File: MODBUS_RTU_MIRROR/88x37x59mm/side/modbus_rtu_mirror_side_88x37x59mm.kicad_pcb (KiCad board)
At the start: 2 copper layers, 52 x 40 mm, 5 parts, among them J1 Conn_01x04_Male, J2 Conn_01x04_Male, U1 ESP32-WROOM-32, U2 TXS0108EPW, U3 AMS1117-3.3

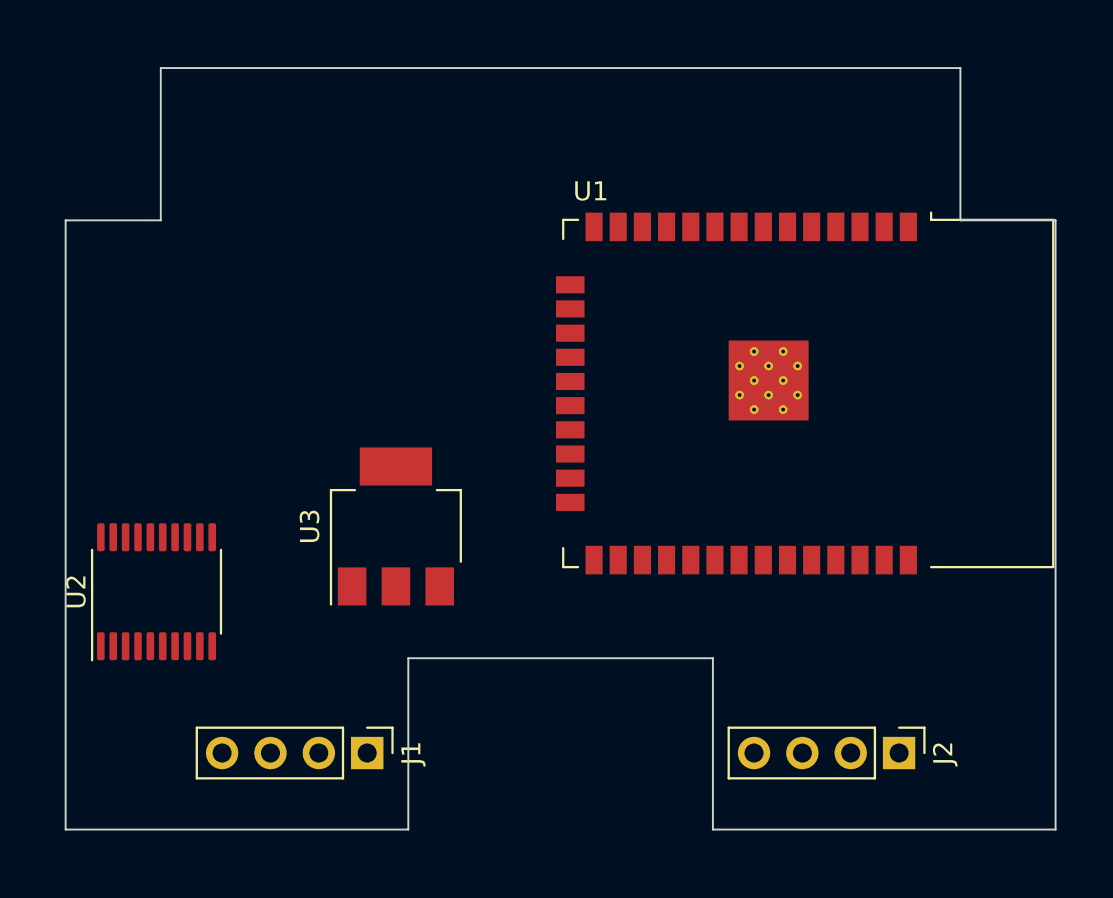
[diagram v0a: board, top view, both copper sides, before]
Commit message: added capacitors, rtc, prog header
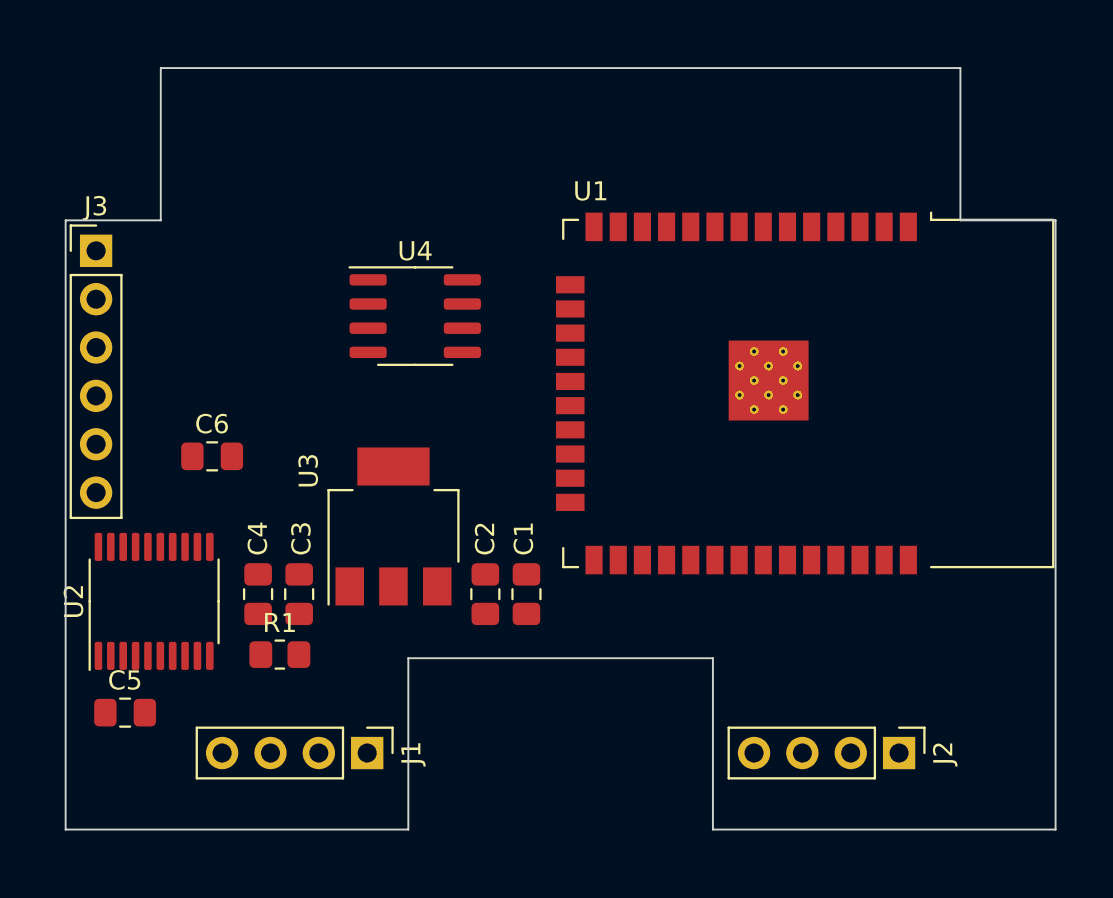
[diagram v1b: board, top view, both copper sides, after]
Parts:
- added C1: 100nF, Capacitor_SMD:C_0805_2012Metric_Pad1.18x1.45mm_HandSolder, F.Cu at (124.2, 127.6)
- added C2: 22uF, Capacitor_SMD:C_0805_2012Metric_Pad1.18x1.45mm_HandSolder, F.Cu at (122.0, 127.6)
- added C3: 22uF, Capacitor_SMD:C_0805_2012Metric_Pad1.18x1.45mm_HandSolder, F.Cu at (112.3, 127.6)
- added C4: 100nF, Capacitor_SMD:C_0805_2012Metric_Pad1.18x1.45mm_HandSolder, F.Cu at (110.1, 127.6)
- added C5: 100nF, Capacitor_SMD:C_0805_2012Metric_Pad1.18x1.45mm_HandSolder, F.Cu at (103.1, 133.9)
- added C6: 100nF, Capacitor_SMD:C_0805_2012Metric_Pad1.18x1.45mm_HandSolder, F.Cu at (107.7, 120.4)
- added J3: Conn_01x06_Male, Connector_PinHeader_2.54mm:PinHeader_1x06_P2.54mm_Vertical, F.Cu at (101.6, 109.6)
- added R1: R, Resistor_SMD:R_0805_2012Metric_Pad1.20x1.40mm_HandSolder, F.Cu at (111.3, 130.8)
- added U4: DS3231MZ, Package_SO:SOIC-8_3.9x4.9mm_P1.27mm, F.Cu at (118.4, 113.0)
- moved U2 0.52 mm to (104.6, 128.0)
- moved U3 0.13 mm to (117.2, 124.1)
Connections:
- U2 pad 10: unconnected-(U2-Pad10) -> Net-(U2-Pad10)

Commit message: added leds and pushbutton
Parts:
- added D1: LED, LED_THT:LED_D3.0mm, F.Cu at (141.7, 104.3)
- added D2: LED, LED_THT:LED_D3.0mm, F.Cu at (136.6, 104.3)
- added D3: LED, LED_THT:LED_D3.0mm, F.Cu at (131.5, 104.3)
- added D4: LED, LED_THT:LED_D3.0mm, F.Cu at (126.4, 104.3)
- added D5: LED, LED_THT:LED_D3.0mm, F.Cu at (121.3, 104.3)
- added D6: LED, LED_THT:LED_D3.0mm, F.Cu at (116.2, 104.3)
- added SW1: SW_Push, Button_Switch_THT:SW_Tactile_SPST_Angled_PTS645Vx31-2LFS, F.Cu at (107.6, 102.9)

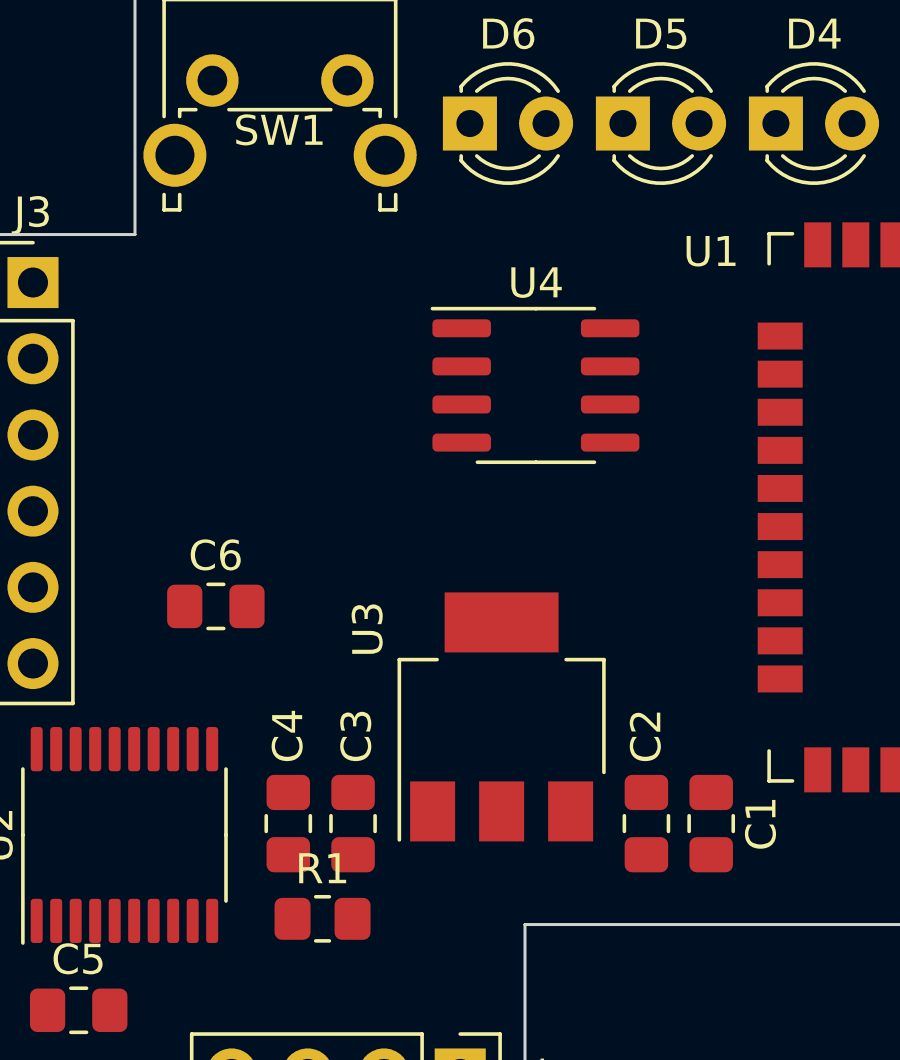
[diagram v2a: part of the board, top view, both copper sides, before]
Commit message: added vertical CR2032 connector
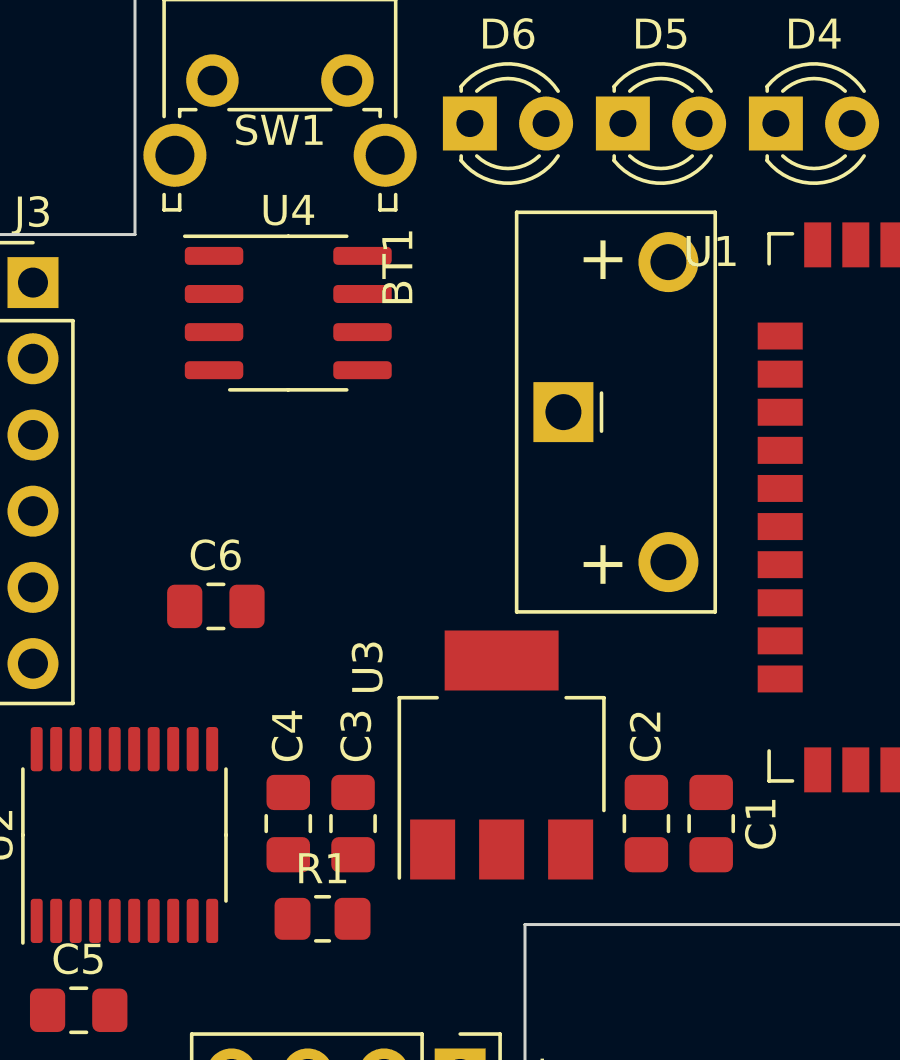
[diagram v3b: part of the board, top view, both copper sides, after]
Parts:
- added BT1: Battery_Cell, Battery_rtc:CR2032_Vertical_CircularHoles, F.Cu at (119.3, 113.9)
- moved U4 8.60 mm to (110.1, 110.6)
- moved U3 1.27 mm to (117.2, 125.3)
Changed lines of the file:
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@@
   (net 87 "unconnected-(D6-Pad1)")
   (net 88 "unconnected-(D6-Pad2)")
+  (net 89 "unconnected-(BT1-Pad1)")
+  (net 90 "unconnected-(BT1-Pad2)")
   (footprint "LED_THT:LED_D3.0mm" (layer "F.Cu")
     (at 131.463 104.3)
@@
       (net 58 "GND") (pintype "passive"))
     (model "${KICAD6_3DMODEL_DIR}/Capacitor_SMD.3dshapes/C_0805_2012Metric.wrl"
+      (offset (xyz 0 0 0))
+      (scale (xyz 1 1 1))
+      (rotate (xyz 0 0 0))
+    )
+  )
+  (footprint "Battery_rtc:CR2032_Vertical_CircularHoles" (layer "F.Cu")
+    (at 119.281 113.919 90)
+    (descr "Panasonic CR-2032/VS1N battery, https://industrial.panasonic.com/cdbs/www-data/pdf2/AAA4000/AAA4000D348.PDF")
+    (tags "battery CR-2032 coin cell vertical")
+    (property "Sheetfile" "modbus_rtu_mirror_side_88x37x59mm.kicad_sch")
+    (property "Sheetname" "")
+    (attr through_hole)
+    (fp_text reference "BT1" (at 4.825 -5.5 90) (layer "F.SilkS")
+      (effects (font (size 1 1) (thickness 0.15)))
+    )
+    (fp_text value "Battery_Cell" (at 4.445 6.35 90) (layer "F.Fab")
+      (effects (font (size 1 1) (thickness 0.15)))
+    )
+    (fp_text user "+" (at 5.08 1.27 90) (layer "F.SilkS")
+      (effects (font (size 1.5 1.5) (thickness 0.15)))
+    )
+    (fp_text user "+" (at -5.08 1.27 90) (layer "F.SilkS")
+      (effects (font (size 1.5 1.5) (thickness 0.15)))
+    )
+    (fp_text user "clearance" (at 9.525 4.445 90 unlocked) (layer "Cmts.User")
+      (effects (font (size 0.5 0.5) (thickness 0.125)))
+    )
+    (fp_text user "Z-AXIS" (at 9.525 -0.635 90 unlocked) (layer "Cmts.User")
+      (effects (font (size 0.5 0.5) (thickness 0.125)))
+    )
+    (fp_text user "MAX 6mm" (at -9.525 1.905 90 unlocked) (layer "Cmts.User")
+      (effects (font (size 0.5 0.5) (thickness 0.125)))
+    )
+    (fp_text user "MAX 6mm" (at 9.525 1.905 90 unlocked) (layer "Cmts.User")
+      (effects (font (size 0.5 0.5) (thickness 0.125)))
+    )
+    (fp_text user "clearance" (at -9.525 4.445 90 unlocked) (layer "Cmts.User")
+      (effects (font (size 0.5 0.5) (thickness 0.125)))
+    )
+    (fp_text user "Z-AXIS" (at -9.525 -0.635 90 unlocked) (layer "Cmts.User")
+      (effects (font (size 0.5 0.5) (thickness 0.125)))
+    )
+    (fp_text user "${REFERENCE}" (at 4.825 -2 90) (layer "F.Fab")
+      (effects (font (size 1 1) (thickness 0.15)))
+    )
+    (fp_line (start -0.635 1.27) (end 0.635 1.27) (layer "F.SilkS") (width 0.12))
+    (fp_line (start -6.66 5.06) (end 6.66 5.06) (layer "F.SilkS") (width 0.12))
+    (fp_line (start -6.66 -1.56) (end 6.66 -1.56) (layer "F.SilkS") (width 0.12))
+    (fp_line (start 6.66 -1.56) (end 6.66 5.06) (layer "F.SilkS") (width 0.12))
+    (fp_line (start -6.66 -1.56) (end -6.66 5.06) (layer "F.SilkS") (width 0.12))
+    (fp_line (start -11.6 5.06) (end 11.6 5.06) (layer "Cmts.User") (width 0.12))
+    (fp_line (start 11.6 -1.45) (end 11.6 5.06) (layer "Cmts.User") (width 0.12))
+    (fp_line (start -11.6 -1.45) (end 11.6 -1.45) (layer "Cmts.User") (width 0.12))
+    (fp_line (start -11.6 -1.45) (end -11.6 5.06) (layer "Cmts.User") (width 0.12))
+    (fp_line (start -6.94 5.34) (end 6.94 5.34) (layer "F.CrtYd") (width 0.05))
+    (fp_line (start 6.94 -1.84) (end 6.94 5.34) (layer "F.CrtYd") (width 0.05))
+    (fp_line (start -6.94 -1.84) (end 6.94 -1.84) (layer "F.CrtYd") (width 0.05))
+    (fp_line (start -6.94 -1.84) (end -6.94 5.34) (layer "F.CrtYd") (width 0.05))
+    (fp_line (start -6.55 -1.45) (end 6.55 -1.45) (layer "F.Fab") (width 0.1))
+    (fp_line (start 6.55 -1.45) (end 6.55 4.95) (layer "F.Fab") (width 0.1))
+    (fp_line (start -6.55 4.95) (end 6.55 4.95) (layer "F.Fab") (width 0.1))
+    (fp_line (start -6.55 -1.45) (end -6.55 4.95) (layer "F.Fab") (width 0.1))
+    (pad "1" thru_hole circle (at 5 3.5 90) (size 2 2) (drill 1.2) (layers *.Cu *.Mask)
+      (net 89 "unconnected-(BT1-Pad1)") (pinfunction "+") (pintype "passive"))
+    (pad "1" thru_hole circle (at -5 3.5 90) (size 2 2) (drill 1.2) (layers *.Cu *.Mask)
+      (net 89 "unconnected-(BT1-Pad1)") (pinfunction "+") (pintype "passive"))
+    (pad "2" thru_hole rect (at 0 0 180) (size 2 2) (drill 1.2) (layers *.Cu *.Mask)
+      (net 90 "unconnected-(BT1-Pad2)") (pinfunction "-") (pintype "passive"))
+    (model "${KICAD6_3DMODEL_DIR}/Battery.3dshapes/Battery_Panasonic_CR2032-VS1N_Vertical_CircularHoles.wrl"
       (offset (xyz 0 0 0))
       (scale (xyz 1 1 1))
@@
   )
   (footprint "Package_SO:SOIC-8_3.9x4.9mm_P1.27mm" (layer "F.Cu")
-    (at 118.364 113.03)
+    (at 110.109 110.617)
     (descr "SOIC, 8 Pin (JEDEC MS-012AA, https://www.analog.com/media/en/package-pcb-resources/package/pkg_pdf/soic_narrow-r/r_8.pdf), generated with kicad-footprint-generator ipc_gullwing_generator.py")
     (tags "SOIC SO")
@@
   )
   (footprint "Package_TO_SOT_SMD:SOT-223-3_TabPin2" (layer "F.Cu")
-    (at 117.221 124.079 90)
+    (at 117.221 125.349 90)
     (descr "module CMS SOT223 4 pins")
     (tags "CMS SOT")

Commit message: all elements placed
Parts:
- added C7: 100nF, Capacitor_SMD:C_0805_2012Metric_Pad1.18x1.45mm_HandSolder, F.Cu at (105.3, 112.5)
- added C8: 100nF, Capacitor_SMD:C_0805_2012Metric_Pad1.18x1.45mm_HandSolder, F.Cu at (106.3, 122.2)
- added C9: 100nF, Capacitor_SMD:C_0805_2012Metric_Pad1.18x1.45mm_HandSolder, F.Cu at (113.8, 120.0)
- added R10: NONE, Resistor_SMD:R_0805_2012Metric_Pad1.20x1.40mm_HandSolder, F.Cu at (109.1, 113.7)
- added R11: 10k, Resistor_SMD:R_0805_2012Metric_Pad1.20x1.40mm_HandSolder, F.Cu at (105.3, 109.9)
- added R12: 4.7k, Resistor_SMD:R_0805_2012Metric_Pad1.20x1.40mm_HandSolder, F.Cu at (113.8, 118.0)
- added R13: 4.7k, Resistor_SMD:R_0805_2012Metric_Pad1.20x1.40mm_HandSolder, F.Cu at (113.8, 116.0)
- added R2: 1k, Resistor_SMD:R_0805_2012Metric_Pad1.20x1.40mm_HandSolder, F.Cu at (144.5, 130.8)
- added R3: 1k, Resistor_SMD:R_0805_2012Metric_Pad1.20x1.40mm_HandSolder, F.Cu at (142.0, 130.8)
- added R4: 1k, Resistor_SMD:R_0805_2012Metric_Pad1.20x1.40mm_HandSolder, F.Cu at (139.3, 130.8)
- added R5: 1k, Resistor_SMD:R_0805_2012Metric_Pad1.20x1.40mm_HandSolder, F.Cu at (136.8, 130.8)
- added R6: 1k, Resistor_SMD:R_0805_2012Metric_Pad1.20x1.40mm_HandSolder, F.Cu at (128.1, 129.7)
- added R7: 1k, Resistor_SMD:R_0805_2012Metric_Pad1.20x1.40mm_HandSolder, F.Cu at (132.6, 129.5)
- added R8: 10k, Resistor_SMD:R_0805_2012Metric_Pad1.20x1.40mm_HandSolder, F.Cu at (109.1, 108.6)
- added R9: 0, Resistor_SMD:R_0805_2012Metric_Pad1.20x1.40mm_HandSolder, F.Cu at (109.1, 111.1)
- added U5: FM24C64C, Package_SO:SOIC-8_3.9x4.9mm_P1.27mm, F.Cu at (107.6, 118.0)
- R1: value R -> 0
- moved J3 12.6 mm to (101.5, 122.2), turned to 180 degrees
- moved U4 12.2 mm to (120.0, 117.7)
- moved C6 4.76 mm to (111.1, 123.7)
- moved BT1 1.48 mm to (118.2, 112.9), turned to 180 degrees
- moved U3 0.25 mm to (117.2, 125.6)
- turned U2 to -90 degrees
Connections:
- BT1 pad 1: unconnected-(BT1-Pad1) -> +BATT
- BT1 pad 2: unconnected-(BT1-Pad2) -> GND
- D1 pad 1: unconnected-(D1-Pad1) -> Net-(D1-Pad1)
- D1 pad 2: unconnected-(D1-Pad2) -> +3.3V
- D2 pad 1: unconnected-(D2-Pad1) -> Net-(D2-Pad1)
- D2 pad 2: unconnected-(D2-Pad2) -> /STP_LED
- D3 pad 1: unconnected-(D3-Pad1) -> Net-(D3-Pad1)
- D3 pad 2: unconnected-(D3-Pad2) -> +3.3V
- D4 pad 1: unconnected-(D4-Pad1) -> Net-(D4-Pad1)
- D4 pad 2: unconnected-(D4-Pad2) -> +3.3V
- D5 pad 1: unconnected-(D5-Pad1) -> Net-(D5-Pad1)
- D5 pad 2: unconnected-(D5-Pad2) -> +3.3V
- D6 pad 1: unconnected-(D6-Pad1) -> Net-(D6-Pad1)
- D6 pad 2: unconnected-(D6-Pad2) -> +3.3V
- J1 pad 1: unconnected-(J1-Pad1) -> Net-(J1-Pad1)
- J1 pad 2: unconnected-(J1-Pad2) -> Net-(J1-Pad2)
- J1 pad 3: unconnected-(J1-Pad3) -> Net-(J1-Pad3)
- J1 pad 4: unconnected-(J1-Pad4) -> Net-(J1-Pad4)
- J2 pad 3: unconnected-(J2-Pad3) -> Net-(J2-Pad3)
- J2 pad 4: unconnected-(J2-Pad4) -> Net-(J2-Pad4)
- J3 pad 1: unconnected-(J3-Pad1) -> GND
- J3 pad 2: unconnected-(J3-Pad2) -> /ESP_TXD
- J3 pad 3: unconnected-(J3-Pad3) -> /ESP_RXD
- J3 pad 4: unconnected-(J3-Pad4) -> +3.3V
- J3 pad 5: unconnected-(J3-Pad5) -> /ESP_EN
- J3 pad 6: unconnected-(J3-Pad6) -> /ESP_IO0
- R1 pad 1: Net-(R1-Pad1) -> +3.3V
- R1 pad 2: GND -> Net-(R1-Pad2)
- SW1 pad 1: unconnected-(SW1-Pad1) -> /STP_SW
- SW1 pad 2: unconnected-(SW1-Pad2) -> GND
- U1 pad 12: unconnected-(U1-Pad12) -> /STP_SW
- U1 pad 25: unconnected-(U1-Pad25) -> /ESP_IO0
- U1 pad 26: unconnected-(U1-Pad26) -> /RX2_LED
- U1 pad 27: unconnected-(U1-Pad27) -> Net-(R10-Pad2)
- U1 pad 28: unconnected-(U1-Pad28) -> /TX2_LED
- U1 pad 3: unconnected-(U1-Pad3) -> /ESP_EN
- U1 pad 30: unconnected-(U1-Pad30) -> /RX1_LED
- U1 pad 31: unconnected-(U1-Pad31) -> Net-(U1-Pad31)
- U1 pad 33: unconnected-(U1-Pad33) -> /TX1_LED
- U1 pad 34: unconnected-(U1-Pad34) -> /ESP_RXD
- U1 pad 35: unconnected-(U1-Pad35) -> /ESP_TXD
- U1 pad 37: unconnected-(U1-Pad37) -> /STP_LED
- U1 pad 8: unconnected-(U1-Pad8) -> /I2C0_SDA
- U1 pad 9: unconnected-(U1-Pad9) -> /I2C0_SCL
- U2 pad 1: unconnected-(U2-Pad1) -> /RX2_LED
- U2 pad 10: Net-(R1-Pad1) -> Net-(R1-Pad2)
- U2 pad 14: unconnected-(U2-Pad14) -> Net-(J1-Pad4)
- U2 pad 15: unconnected-(U2-Pad15) -> Net-(J1-Pad3)
- U2 pad 16: unconnected-(U2-Pad16) -> Net-(J1-Pad2)
- U2 pad 17: unconnected-(U2-Pad17) -> Net-(J1-Pad1)
- U2 pad 18: unconnected-(U2-Pad18) -> Net-(J2-Pad4)
- U2 pad 19: +3.3V -> +5V
- U2 pad 2: +5V -> +3.3V
- U2 pad 20: unconnected-(U2-Pad20) -> Net-(J2-Pad3)
- U2 pad 3: unconnected-(U2-Pad3) -> Net-(R10-Pad1)
- U2 pad 4: unconnected-(U2-Pad4) -> /TX2_LED
- U2 pad 5: unconnected-(U2-Pad5) -> /RX1_LED
- U2 pad 6: unconnected-(U2-Pad6) -> Net-(U1-Pad31)
- U2 pad 7: unconnected-(U2-Pad7) -> /TX1_LED
- U4 pad 2: unconnected-(U4-Pad2) -> +3.3V
- U4 pad 5: unconnected-(U4-Pad5) -> GND
- U4 pad 6: unconnected-(U4-Pad6) -> +BATT
- U4 pad 7: unconnected-(U4-Pad7) -> /I2C0_SDA
- U4 pad 8: unconnected-(U4-Pad8) -> /I2C0_SCL
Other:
- outline, holes or cut-outs redrawn
